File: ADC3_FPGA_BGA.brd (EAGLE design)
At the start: 40 x 40 mm, 80 parts, among them CON1 MEZZANINE_2X30, CON2 MEZZANINE_2X30, CON3 USB-SC, IC1 3.3V, IC2 MPM3804, IC3 1.0V, IC4 LFD2NX-40, IC5 EEPROM, IC6 93LC56, IC7 FT2232H, IC8 HyperRAM, J1 CLK, X1 25MHz, X2 12MHz

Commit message: Artix-7 途中
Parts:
- removed X2: 12MHz, my_rcl:KC3225
- added C36, C37, C38: 1u, my_rcl:1005
- added C39, C41, C42, C43, C47, C48, C49, C51: 0.1u, my_rcl:1608
- added C40, C46: 10u, my_rcl:1608
- added C44, C45: 22p, my_rcl:1608
- added C50: 10u, my_rcl:2012
- added D6: PWR, my_rcl:D1608
- added FB8: DRAM, my_rcl:1608-J
- added IC9: HyperRAM, my_ic:TFBGA24
- added J2: BANK35, my_rcl:2012-3-J
- added R20: 1k, my_rcl:1608
- added TP1: TMS, my_connector:TESTPAD
- added TP2: TDI, my_connector:TESTPAD
- added TP3: TCK, my_connector:TESTPAD
- added TP4: TDO, my_connector:TESTPAD
- added TP5: GND, my_connector:TESTPAD
- C10, C11, C13, C34: value 10u -> 1u; device my_rcl:2012 -> my_rcl:1005
- C12, C14, C15: value 0.1u -> 1u
- C16, C17, C18: value 0.1u -> 10u; device my_rcl:1005 -> my_rcl:1608
- C19, C4: value 0.1u -> 10u
- C2, C24: device my_rcl:1608 -> my_rcl:2012
- C20, C21, C23: value 0.1u -> 10u; device my_rcl:1005 -> my_rcl:2012
- C22, C25: value 0.1u -> 10u; device my_rcl:1608 -> my_rcl:2012
- C26, C27, C31, C32, C33, C35: value 0.1u -> 1u; device my_rcl:1608 -> my_rcl:1005
- C28, C29: value 22p -> 1u; device my_rcl:1608 -> my_rcl:1005
- C30, C9: value 10u -> 1u; device my_rcl:1608 -> my_rcl:1005
- C5: value 10u -> 0.1u
- C7, C8: device my_rcl:1608 -> my_rcl:1005
- D5: value PWR -> LED2
- FB3, IC3: value 1.0V -> 2.5V
- FB5: value FT -> 1.0V
- FB7: value DRAM -> FT
- IC1: value 3.3V -> ARTIX7-FTG256; device my_ic:SOT23-5 -> my_ic:FTG256
- IC2: value MPM3804 -> 3.3V; device my_ic:QFN-10 -> my_ic:SOT23-5
- IC4: value LFD2NX-40 -> MPM3804; device my_ic:CABGA192 -> my_ic:QFN-10
- IC5: value EEPROM -> MPM3804; device my_ic:SOP8 -> my_ic:QFN-10
- IC6: value 93LC56 -> EEPROM; device my_ic:SOT23-6 -> my_ic:SOIC-SOIJ-8
- IC7: value FT2232H -> 93LC56; device my_ic:VQFN56 -> my_ic:SOT23-6
- IC8: value HyperRAM -> FT2232H-2; device my_ic:TFBGA24 -> my_ic:QFN56-HT
- J1: value CLK -> BANK34; device my_rcl:1608-J -> my_rcl:2012-3-J
- R12, R3: value 10k -> 1k
- R13: value 1k -> 12.1k
- R14: value 12.1k -> 1k
- R4: value 10k -> 1.5k
- X1: value 25MHz -> 12MHz
- moved FB7 51.0 mm to (4.00, -22.2), flipped to the bottom, turned to 90 degrees
- moved IC8 40.3 mm to (1.50, -15.0)
- moved R7 40.3 mm to (13.5, -9.75), turned to 0 degrees
- moved C16 37.7 mm to (-7.00, -24.0), turned to 180 degrees
- moved C18 37.0 mm to (-13.0, -19.5), flipped to the top, turned to 0 degrees
- moved C9 36.1 mm to (1.00, 3.50), flipped to the bottom, turned to 0 degrees
- moved C35 34.8 mm to (7.00, 0.00)
- moved C2 32.6 mm to (-3.00, -21.5), turned to 90 degrees
- moved FB1 31.6 mm to (-2.50, -22.5), flipped to the top, turned to 270 degrees
- moved X1 31.5 mm to (9.25, -20.5), flipped to the top, turned to 0 degrees
- moved C10 31.2 mm to (1.00, 5.50), flipped to the bottom, turned to 0 degrees
- moved IC4 31.0 mm to (-13.5, -22.5), turned to 90 degrees
- moved C13 30.8 mm to (0.00, 0.50), flipped to the bottom, turned to 0 degrees
- moved C31 30.5 mm to (7.00, 7.50), turned to 0 degrees
- moved C8 30.4 mm to (3.00, -0.50), turned to 0 degrees
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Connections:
- removed net +1V0_LDO: C8.1, FB3.1, IC3.5
- removed net +3.3V_LDO: C7.1, FB2.1, IC1.5
- removed net ADC_DN1: CON1.30, IC4.H14
- removed net ADC_DP1: CON1.28, IC4.H13
- removed net INITN: IC4.B2, R8.1
- removed net JTAG_EN: IC4.A13, R7.1
- removed net N$6: J1.1, X1.3
- removed net N$7: IC2.9, R1.1, R2.2
- removed net PB10A: CON2.7, IC4.L2
- removed net PB10B: CON2.3, IC4.M2
- removed net PB12A: CON2.6, IC4.P2
- removed net PB12B: CON2.4, IC4.P3
- removed net PB4A: CON2.13, IC4.K1
- removed net PB4B: CON2.9, IC4.L1
- removed net PB58A: CON1.3, IC4.P9
- removed net PB58B: CON1.5, IC4.N9
- removed net PB60A: CON1.7, IC4.P10
- removed net PB60B: CON1.9, IC4.N10
- removed net PB64A: CON1.17, IC4.M9
- removed net PB64B: CON1.21, IC4.L9
- removed net PB66A: CON1.29, IC4.K9
- removed net PB66B: CON1.27, IC4.K10
- removed net PB68A: CON1.15, IC4.M11
- removed net PB68B: CON1.19, IC4.L12
- removed net PB6A: CON2.12, IC4.K3
- removed net PB6B: CON2.10, IC4.L3
- removed net PB70A: CON1.25, IC4.K11
- removed net PB70B: CON1.23, IC4.K12
- removed net PB72A: CON1.11, IC4.P11
- removed net PB72B: CON1.13, IC4.N11
- removed net PB74A: CON1.4, IC4.P12
- removed net PB74B: CON1.6, IC4.P13
- removed net PB76A: CON1.8, IC4.N13
- removed net PB76B: CON1.10, IC4.N14
- removed net PB78A: CON1.14, IC4.M14
- removed net PB78B: CON1.12, IC4.M13
- removed net PB80A: CON1.16, IC4.L13
- removed net PB80B: CON1.18, IC4.L14
- removed net PB82A: CON1.20, IC4.K13
- removed net PB82B: CON1.22, IC4.K14
- removed net PB84A: CON1.26, IC4.J14
- removed net PB84B: CON1.24, IC4.J13
- removed net PB8A: CON2.5, IC4.M1
- removed net PB8B: CON2.8, IC4.N1
- removed net PL24A: CON2.30, IC4.E2
- removed net PL24B: CON2.32, IC4.E1
- removed net PL26A: CON2.28, IC4.F3
- removed net PL26B: CON2.26, IC4.F4
- removed net PL30A: CON2.29, IC4.F2, J1.2
- removed net PL30B: CON2.31, IC4.F1
- removed net PL32A: CON2.27, IC4.G1
- removed net PL32B: CON2.25, IC4.G2
- removed net PL36A: CON2.23, IC4.H1
- removed net PL36B: CON2.21, IC4.H2
- removed net PL38A: CON2.24, IC4.H3
- removed net PL38B: CON2.22, IC4.H4
- removed net PL42A: CON2.19, IC4.J1
- removed net PL42B: CON2.17, IC4.J2
- removed net PL44A: CON2.20, IC4.J3
- removed net PL44B: CON2.18, IC4.J4
- removed net PL47A: CON2.11, IC4.K2
- removed net PR13B: CON1.51, IC4.A12
- removed net PR17A: CON1.49, IC4.A10
- removed net PR24A: CON1.46, IC4.D14
- removed net PR24B: CON1.50, IC4.C14
- removed net PR26A: CON1.47, IC4.C11
- removed net PR27A: CON1.48, IC4.D12
- removed net PR27B: CON1.39, IC4.E12
- removed net PR30A: CON1.45, IC4.E9
- removed net PR30B: CON1.41, IC4.E10
- removed net PR32A: CON1.43, IC4.D11
- removed net PR32B: CON1.37, IC4.E11
- removed net PR34A: CON1.40, IC4.F13
- removed net PR34B: CON1.38, IC4.F14
- removed net PR36A: CON1.44, IC4.E13
- removed net PR36B: CON1.42, IC4.E14
- removed net PR38A: CON1.34, IC4.G14
- removed net PR38B: CON1.36, IC4.G13
- removed net PR42A: CON1.35, IC4.F11
- removed net PR42B: CON1.33, IC4.G12
- removed net PROGRAMN: IC4.A2, R9.1
- new net +1V0_DCDC: C19.1, FB5.1, IC5.6, IC5.7, IC5.8, R3.2
- new net +1V0_DCDC_FB: IC5.9, R3.1, R4.2
- new net +1V8_DCDC_FB: IC4.9, R1.1, R2.2
- new net +2V5: C21.1, CON2.49, CON2.50, FB3.2, J1.3, J2.3
- new net +2V5_LDO: C17.1, FB3.1, IC3.5
- new net +3V3_LDO: C16.1, FB2.1, IC2.5
- new net 1.0V_DCDC_SW: IC5.2, IC5.3, IC5.4
- new net INIT_B: IC1.K10, R7.1
- new net IO0_14: CON2.26, IC1.K12
- new net IO10N_15: CON2.7, IC1.B16
- new net IO10N_35: CON1.16, IC1.D1
- new net IO10P_15: CON2.9, IC1.C16
- new net IO10P_35: CON1.18, IC1.E2
- new net IO11N_14: CON2.40, IC1.P13
- new net IO11P_14: CON2.38, IC1.N13
- new net IO12N_14: CON2.32, IC1.P14
- new net IO12N_35: CON1.19, IC1.C4
- new net IO12P_14: CON2.30, IC1.N14
- new net IO12P_35: CON1.21, IC1.D4
- new net IO13N_15: CON2.12, IC1.E13
- new net IO13P_15: CON2.14, IC1.E12
- new net IO14N_35: CON1.23, IC1.F3
- new net IO14P_35: CON1.25, IC1.F4
- new net IO15N_15: CON2.10, IC1.D15
- new net IO15N_35: CON1.20, IC1.E1
- new net IO15P_15: CON2.8, IC1.D14
- new net IO15P_35: CON1.22, IC1.F2
- new net IO17N_15: CON2.11, IC1.D16
- new net IO17N_35: CON1.24, IC1.G1
- new net IO17P_15: CON2.13, IC1.E16
- new net IO17P_35: CON1.26, IC1.G2
- new net IO19N_35: CON1.35, IC1.J4
- new net IO19P_35: CON1.37, IC1.J5
- new net IO20N_35: CON1.28, IC1.H1
- new net IO20P_35: CON1.30, IC1.H2
- new net IO21N_15: CON2.16, IC1.F14
- new net IO21N_35: CON1.27, IC1.H3
- new net IO21P_15: CON2.18, IC1.G14
- new net IO21P_35: CON1.29, IC1.J3
- new net IO22N_15: CON2.15, IC1.G16
- new net IO22N_35: CON1.32, IC1.J1
- new net IO22P_15: CON2.17, IC1.H16
- new net IO22P_35: CON1.34, IC1.K1
- new net IO23N_15: CON2.21, IC1.J16
- new net IO23N_35: CON1.38, IC1.L2
- new net IO23P_15: CON2.19, IC1.J15
- new net IO23P_35: CON1.36, IC1.L3
- new net IO24N_15: CON2.20, IC1.G15
- new net IO24N_35: CON1.31, IC1.K2
- new net IO24P_15: CON2.22, IC1.H14
- new net IO24P_35: CON1.33, IC1.K3
- new net IO2N_14: CON2.27, IC1.K16
- new net IO2N_34: CON1.42, IC1.M1
- new net IO2N_35: CON1.9, IC1.B5
- new net IO2P_14: CON2.25, IC1.K15
- new net IO2P_34: CON1.44, IC1.M2
- new net IO2P_35: CON1.7, IC1.B6
- new net IO3N_35: CON1.6, IC1.A4
- new net IO3P_35: CON1.4, IC1.A5
- new net IO4N_14: CON2.31, IC1.M14
- new net IO4N_34: CON1.48, IC1.P1
- new net IO4N_35: CON1.11, IC1.A3
- new net IO4P_14: CON2.29, IC1.L14
- new net IO4P_34: CON1.46, IC1.N1
- new net IO4P_35: CON1.13, IC1.B4
- new net IO5N_34: CON1.43, IC1.P3
- new net IO5N_35: CON1.5, IC1.C6
- new net IO5P_14: CON2.28, IC1.K13
- new net IO5P_34: CON1.41, IC1.P4
- new net IO5P_35: CON1.3, IC1.C7
- new net IO7N_14: CON2.35, IC1.N16
- new net IO7N_34: CON1.50, IC1.R1
- new net IO7N_35: CON1.15, IC1.C2
- new net IO7P_14: CON2.33, IC1.M16
- new net IO7P_34: CON1.52, IC1.R2
- new net IO7P_35: CON1.17, IC1.C3
- new net IO8N_14: CON2.39, IC1.P16
- new net IO8N_15: CON2.4, IC1.B14
- new net IO8N_34: CON1.47, IC1.T2
- new net IO8N_35: CON1.8, IC1.A2
- new net IO8P_14: CON2.37, IC1.P15
- new net IO8P_15: CON2.6, IC1.C14
- new net IO8P_34: CON1.45, IC1.R3
- new net IO8P_35: CON1.10, IC1.B2
- new net IO9N_14: CON2.36, IC1.R16
- new net IO9N_15: CON2.3, IC1.A15
- new net IO9N_34: CON1.49, IC1.T3
- new net IO9N_35: CON1.12, IC1.B1
- new net IO9P_14: CON2.34, IC1.R15
- new net IO9P_15: CON2.5, IC1.B15
- new net IO9P_34: CON1.51, IC1.T4
- new net IO9P_35: CON1.14, IC1.C1
- new net LED3: D5.A, IC1.R5
- new net N$5: D5.K, R18.2
- new net PROGRAM_B: IC1.L9, R8.1
- new net VCCO34: C24.1, C26.1, C28.1, IC1.M3, IC1.R4, IC1.T1, J1.2
- new net VCCO35: C25.1, C27.1, C29.1, C30.1, IC1.A6, IC1.B3, IC1.D7, IC1.E4, IC1.F1, IC1.J2, J2.2
- net +1V0: now also C13.1, C23.1, C7.1, C9.1, FB5.2, IC1.E10, IC1.F11, IC1.F7, IC1.F9, IC1.G6, IC1.H9, IC1.J6, IC1.K9, IC1.L8; no longer C12.1, C17.1, FB3.2, IC4.F9, IC4.G7, IC4.H9, IC4.J7, IC4.J9
- net +1V8: now also C10.1, C12.1, C22.1, C31.1, C33.1, C35.1, C8.1, FB7.1, FB8.2, IC1.A16, IC1.B13, IC1.C10, IC1.E14, IC1.G10, IC1.G8, IC1.H15, IC1.J10, IC1.J12, IC1.K11, IC1.L10; no longer C13.1, C16.1, C18.1, C23.1, C6.1, FB6.1, FB7.2, IC3.1, IC3.3, IC4.F7, IC4.G9, IC4.H10, IC4.H7, IC4.J10, IC4.J12, IC4.L11, IC4.L5, IC4.M10, IC4.M3, IC4.M6, IC4.N12, IC4.N3
- net +1V8_DCDC: now also C18.1, IC4.6, IC4.7, IC4.8; no longer C9.1, IC2.6, IC2.7, IC2.8
- net +3V3: now also C32.1, C34.1, C36.1, C37.1, C38.1, C39.1, D6.A, FB6.1, IC1.E7, IC1.L15, IC1.L16, IC1.L6, IC1.M13, IC1.M9, IC1.N10, IC1.P7, IC1.R14, IC1.T11, IC6.3, IC6.7, IC6.8, J1.1, J2.1, R5.2; no longer C10.1, C19.1, C21.1, C22.1, CON2.49, CON2.50, D5.A, FB5.1, IC4.C12, IC4.C7, IC4.E4, IC4.G11, IC4.G4, IC5.3, IC5.7, IC5.8, R11.2, R3.2, R4.2, X1.1, X1.4
- net 1.8V_DCDC_SW: now also IC4.2, IC4.3, IC4.4; no longer IC2.2, IC2.3, IC2.4
- net DONE: now also IC1.H10, R9.1; no longer IC4.A3, R10.1
- net DRAM_+1V8: now also C49.1, C50.1, C51.1, FB8.1, IC9.B4, IC9.D1, IC9.E4, R20.2; no longer C33.1, C34.1, C35.1, FB7.1, IC8.B4, IC8.D1, IC8.E4
- net DRAM_CKN: now also IC1.A9, IC9.B1; no longer IC4.L7, IC8.B1
- net DRAM_CKP: now also IC1.A8, IC9.B2; no longer IC4.M7, IC8.B2
- net DRAM_CS: now also IC1.C8, IC9.A3; no longer IC4.K6, IC8.A3
- net DRAM_DQ0: now also IC1.A10, IC9.D3; no longer IC4.N5, IC8.D3
- net DRAM_DQ1: now also IC1.B11, IC9.D2; no longer IC4.P7, IC8.D2
- net DRAM_DQ2: now also IC1.A13, IC9.C4; no longer IC4.P4, IC8.C4
- net DRAM_DQ3: now also IC1.C13, IC9.D4; no longer IC4.N4, IC8.D4
- net DRAM_DQ4: now also IC1.A14, IC9.D5; no longer IC4.M4, IC8.D5
- net DRAM_DQ5: now also IC1.C12, IC9.E3; no longer IC4.P5, IC8.E3
- net DRAM_DQ6: now also IC1.A12, IC9.E2; no longer IC4.P6, IC8.E2
- net DRAM_DQ7: now also IC1.B12, IC9.E1; no longer IC4.N6, IC8.E1
- net DRAM_NRST: now also IC9.A4, R20.1; no longer IC4.K5, IC8.A4
- net DRAM_RWDS: now also IC1.B10, IC9.C3; no longer IC4.N7, IC8.C3
- net FLASH_CS: now also IC1.L12, IC6.1, R10.1; no longer IC4.B4, IC5.1, R11.1
- net FLASH_MISO: now also IC1.J14, IC6.2; no longer IC4.A5, IC5.2
- net FLASH_MOSI: now also IC1.J13, IC6.5; no longer IC4.A4, IC5.5
- net FLASH_SCK: now also IC1.E8, IC6.6; no longer IC4.B3, IC5.6
- net FT_+1V8: now also C46.1, C47.1, C48.1, FB7.2, IC8.2, IC8.31; no longer C30.1, C31.1, C32.1, FB6.2, IC7.2, IC7.31
- net FT_+3V3: now also C40.1, C41.1, C42.1, C43.1, FB6.2, IC7.6, IC8.16, IC8.36, IC8.5, IC8.50, IC8.9, R11.1, R14.1; no longer C24.1, C25.1, C26.1, C27.1, FB5.2, IC6.6, IC7.16, IC7.36, IC7.5, IC7.50, IC7.9, R12.1, R15.1
- net FT_CLK: now also IC1.N11, IC8.27; no longer IC4.D7, IC7.27
- net FT_D0: now also IC1.T15, IC8.12; no longer IC4.E3, IC7.12
- net FT_D1: now also IC1.T14, IC8.13; no longer IC4.D2, IC7.13
- net FT_D2: now also IC1.R13, IC8.14; no longer IC4.D1, IC7.14
- net FT_D3: now also IC1.T13, IC8.15; no longer IC4.D3, IC7.15
- net FT_D4: now also IC1.R12, IC8.17; no longer IC4.C1, IC7.17
- net FT_D5: now also IC1.T12, IC8.18; no longer IC4.C2, IC7.18
- net FT_D6: now also IC1.R11, IC8.19; no longer IC4.B1, IC7.19
- net FT_D7: now also IC1.R10, IC8.20; no longer IC4.C3, IC7.20
- net FT_NOE: now also IC1.T7, IC8.28; no longer IC4.D6, IC7.28
- net FT_NRD: now also IC1.P8, IC8.24; no longer IC4.C5, IC7.24
- net FT_NWR: now also IC1.T8, IC8.25; no longer IC4.C6, IC7.25
- net FT_RXNF: now also IC1.T10, IC8.22; no longer IC4.C4, IC7.22
- net FT_SIWU: now also IC1.R8, IC8.26; no longer IC4.D5, IC7.26
- net FT_TXNE: now also IC1.T9, IC8.23; no longer IC4.B5, IC7.23
- net GND: now also C36.2, C37.2, C38.2, C39.2, C40.2, C41.2, C42.2, C43.2, C44.2, C45.2, C46.2, C47.2, C48.2, C49.2, C50.2, C51.2, CON1.39, CON1.40, CON2.23, CON2.24, IC1.A1, IC1.A11, IC1.B8, IC1.C15, IC1.C5, IC1.D12, IC1.D2, IC1.E9, IC1.F10, IC1.F16, IC1.F6, IC1.F8, IC1.G13, IC1.G3, IC1.G7, IC1.G9, IC1.H6, IC1.H7, IC1.H8, IC1.J11, IC1.J7, IC1.J8, IC1.J9, IC1.K14, IC1.K4, IC1.K6, IC1.K7, IC1.K8, IC1.L1, IC1.L11, IC1.M10, IC1.M11, IC1.M8, IC1.N15, IC1.N5, IC1.P12, IC1.P2, IC1.R9, IC1.T16, IC1.T6, IC2.2, IC4.10, IC5.10, IC6.4, IC7.2, IC8.10, IC8.21, IC8.41, IC8.45, IC8.HT, IC9.B3, IC9.C1, IC9.E5, R13.2, R15.1, R4.1, TP5.1, X1.4; no longer CON1.31, CON1.32, CON1.52, CON2.14, CON2.15, CON2.16, CON2.33, CON2.34, CON2.35, CON2.36, CON2.37, CON2.38, CON2.39, CON2.40, IC1.2, IC2.10, IC4.A1, IC4.A14, IC4.B11, IC4.B6, IC4.D4, IC4.F12, IC4.F8, IC4.G3, IC4.G8, IC4.H8, IC4.J11, IC4.J8, IC4.L10, IC4.M12, IC4.M5, IC4.N2, IC4.P1, IC4.P14, IC5.4, IC6.2, IC7.10, IC7.21, IC7.41, IC7.45, IC7.HT, IC8.B3, IC8.C1, IC8.E5, R14.2, R5.1, X2.2, X2.4
- net JTAG_TCK: now also IC1.L7, IC8.32, TP3.1; no longer IC4.A11, IC7.32, R5.2
- net JTAG_TDI: now also IC1.N7, IC8.33, R5.1, TP2.1; no longer IC4.D9, IC7.33, R4.1
- net JTAG_TDO: now also IC1.N8, IC8.34, TP4.1; no longer IC4.D10, IC7.34, R3.1
- net JTAG_TMS: now also IC1.M7, IC8.35, TP1.1; no longer IC4.E8, IC7.35
- net LED0: now also IC1.R7; no longer IC4.B13
- net LED1: now also IC1.R6; no longer IC4.B14
- net LED2: now also IC1.T5; no longer IC4.B12
- net N$1: now also D6.K; no longer D5.K
- net N$10: now also IC7.3, IC8.55, R12.2; no longer IC6.3, IC7.55, R13.2
- net N$11: now also IC7.5, IC8.1; no longer IC6.5, IC7.1
- net N$12: now also IC7.1, R11.2, R12.1; no longer IC6.1, R12.2, R13.1
- net N$13: now also C45.1, IC8.4, X1.3; no longer C29.1, IC7.4, X2.3
- net N$14: now also C44.1, IC8.3, X1.1; no longer C28.1, IC7.3, X2.1
- net N$15: now also IC8.6, R13.1; no longer IC7.6, R14.1
- net N$16: now also IC8.11, R14.2; no longer IC7.11, R15.2
- net N$2: now also R15.2; no longer R16.2
- net N$3: now also R16.2; no longer R17.2
- net N$4: now also R17.2; no longer R18.2
- net N$9: now also IC7.4, IC8.56; no longer IC6.4, IC7.56
- net USB_DM: now also IC8.7; no longer IC7.7
- net USB_DP: now also IC8.8; no longer IC7.8
- net VIN_DCDC: now also C6.1, IC2.3, IC3.1, IC3.3, IC4.1, IC4.5, IC5.1, IC5.5; no longer IC1.1, IC1.3, IC2.5
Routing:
- net +1V8: track 242.0 -> 69.9 mm, vias 24 -> 13
- net +3V3: track 223.2 -> 95.1 mm, vias 11 -> 14
- net VIN: track 96.2 -> 0.00 mm, vias 4 -> 0
- net VCCO35: track 0.00 -> 32.1 mm, vias 0 -> 7
- net FT_+3V3: track 73.1 -> 44.5 mm, vias 8 -> 6
- net FLASH_SCK: track 11.7 -> 37.4 mm
- net +2V5: track 0.00 -> 25.2 mm, vias 0 -> 2
- net VCCO34: track 0.00 -> 23.7 mm, vias 0 -> 4
- net VIN_DCDC: track 24.9 -> 47.1 mm, vias 3 -> 4
- net INIT_B: track 0.00 -> 20.4 mm, vias 0 -> 2
- net PROGRAMN: track 19.9 -> 0.00 mm, vias 2 -> 0
- net PROGRAM_B: track 0.00 -> 17.8 mm, vias 0 -> 2
- net INITN: track 17.8 -> 0.00 mm, vias 2 -> 0
- net FLASH_MISO: track 13.3 -> 31.0 mm
- net FT_+1V8: track 45.7 -> 28.3 mm, vias 3 -> 2
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- removed copper zone on layer 2, net GND
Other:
- board size 40 x 40 mm -> 40.2 x 45 mm

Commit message: via打てば終わり
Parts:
- D2: value LED0 -> 0
- D3: value LED1 -> 1
- D4: value LED2 -> 2
- D5: value LED2 -> 3
- D6: value PWR -> P
- IC8: value FT2232H-2 -> FT2232H
- moved FB7 14.0 mm to (-5.50, -12.0), turned to 180 degrees
- moved C1 4.75 mm to (17.0, -22.8)
- moved D1 3.26 mm to (13.0, -22.8), turned to 180 degrees
- moved FB3 2.70 mm to (-17.8, -21.5)
- moved FB6 1.41 mm to (0.75, -21.2), turned to 180 degrees
- moved C28 1.25 mm to (-5.00, -3.75)
- moved C50 0.75 mm to (8.25, 13.5)
- moved FB1 0.50 mm to (-3.00, -22.5), turned to 90 degrees
- moved C5 0.25 mm to (-7.00, -18.0)
- moved C6 0.25 mm to (-13.0, -18.0)
- moved FB2 0.25 mm to (-9.75, -22.8)
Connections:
- net +1V8: no longer CON1.55, CON1.56
- net +2V5: now also CON1.55, CON1.56; no longer CON2.49, CON2.50
- net +3V3: now also CON2.49, CON2.50
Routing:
- net VIN: track 0.00 -> 45.5 mm, vias 0 -> 1
- net +1V8: track 69.9 -> 31.3 mm, vias 13 -> 17
- net +1V0: track 36.4 -> 4.79 mm, vias 10 -> 11
- net +3V3: track 95.1 -> 64.5 mm, vias 14 -> 22
- net VCCO35: track 32.1 -> 6.66 mm
- net VCCO34: track 23.7 -> 5.06 mm
- net USB_+5V: track 0.00 -> 5.43 mm, vias 0 -> 2
- net +2V5_LDO: track 3.42 -> 6.30 mm
- net +2V5: track 25.2 -> 22.7 mm, vias 2 -> 3
- net FLASH_CS: track 31.8 -> 33.9 mm
- net IO8P_14: track 13.5 -> 14.9 mm
- net IO8N_14: track 12.2 -> 13.6 mm
- net IO4P_14: track 14.6 -> 16.0 mm
- net IO4N_14: track 14.7 -> 16.1 mm
- added copper zone on layer 3, net +1V0
- added copper zone on layer 14, net +1V8
- added copper zone on layer 3, net +2V5
- added copper zone on layer 14, net +3V3
- added copper zone on layer 2, net GND
- added copper zone on layer 3, net VCCO34
- added copper zone on layer 3, net VCCO35
- removed copper zone on layer 14, net GND
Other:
- board size 40.2 x 45 mm -> 40.4 x 44.4 mm
- board text added: "FPGA Core Board ver2"
- board text removed: "FPGA Core Board ver1"

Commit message: 発注
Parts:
- added C52, C53, C54: 10u, my_rcl:2012
- C11, C12: value 1u -> 0.1u; device my_rcl:1005 -> my_rcl:1608
- C16, C4: value 10u -> 1u; device my_rcl:1608 -> my_rcl:1005
- C20: device my_rcl:2012 -> my_rcl:1608
- C26: value 1u -> 10u; device my_rcl:1005 -> my_rcl:2012
- C39, C5: value 0.1u -> 1u; device my_rcl:1608 -> my_rcl:1005
- C40: value 10u -> 0.1u
- C41, C47, C6: value 0.1u -> 10u
- C44: value 22p -> 0.1u
- C46: value 10u -> 22p
- C50: value 10u -> 0.1u; device my_rcl:2012 -> my_rcl:1608
- R11: value 10k -> 1k
- R13: value 12.1k -> 10k
- R17: value 1k -> 12.1k
- moved C49 31.5 mm to (4.50, -18.0), turned to 0 degrees
- moved C16 27.2 mm to (-1.00, 2.50)
- moved C12 25.2 mm to (-13.0, -18.0), turned to 0 degrees
- moved R18 24.3 mm to (9.00, -13.0), turned to 180 degrees
- moved C4 23.6 mm to (-2.50, -1.00), flipped to the bottom, turned to 270 degrees
- moved R14 22.6 mm to (-13.5, -15.0), turned to 90 degrees
- moved R17 22.5 mm to (9.00, -16.2), turned to 0 degrees
- moved C39 21.7 mm to (1.50, -4.25), turned to 90 degrees
- moved C5 20.2 mm to (3.00, -0.50)
- moved C11 19.9 mm to (-7.00, -18.0)
- moved C25 18.7 mm to (-13.0, -17.8)
- moved C23 17.4 mm to (-17.2, -4.50)
- moved C32 15.5 mm to (7.00, 7.50), turned to 0 degrees
- moved R12 15.1 mm to (-11.8, -15.0), turned to 90 degrees
- moved R16 15.1 mm to (1.50, -22.2), turned to 270 degrees
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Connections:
- net +1V0: now also C16.1, C26.1, C4.1, C53.1; no longer C11.1, C23.1
- net +1V0_DCDC: now also C20.1; no longer C19.1
- net +1V8: now also C25.1, C32.1, C34.1, C36.1, C5.1, C54.1; no longer C12.1, C22.1, C31.1, C33.1, C35.1
- net +1V8_DCDC: now also C19.1; no longer C18.1
- net +2V5: now also C22.1; no longer C21.1
- net +2V5_LDO: now also C18.1; no longer C17.1
- net +3V3: now also C21.1, C33.1, C35.1, C40.1; no longer C20.1, C32.1, C34.1, C36.1
- net +3V3_LDO: now also C17.1; no longer C16.1
- net DRAM_+1V8: now also C52.1; no longer C49.1
- net FT_+1V8: now also C49.1; no longer C46.1
- net FT_+3V3: now also C44.1, R13.1, R18.1; no longer C40.1, R11.1, R14.1
- net GND: now also C52.2, C53.2, C54.2, R11.1, R12.1, R14.1, R17.2; no longer R13.2, R16.1, R17.1, R18.1
- net N$10: now also R16.2; no longer R12.2
- net N$12: now also R13.2, R16.1; no longer R11.2, R12.1
- net N$13: now also C46.1; no longer C45.1
- net N$14: now also C45.1; no longer C44.1
- net N$15: now also R17.1; no longer R13.1
- net N$16: now also R18.2; no longer R14.2
- net N$2: now also R11.2; no longer R15.2
- net N$3: now also R12.2; no longer R16.2
- net N$4: now also R14.2; no longer R17.2
- net N$5: now also R15.2; no longer R18.2
- net VCCO34: now also C23.1, C27.1, C29.1; no longer C24.1, C26.1, C28.1
- net VCCO35: now also C24.1, C28.1, C31.1; no longer C25.1, C27.1, C29.1
- net VIN_DCDC: now also C11.1, C12.1; no longer C4.1, C5.1
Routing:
- net +1V8: track 31.3 -> 34.1 mm
- net +1V0: track 4.79 -> 7.57 mm

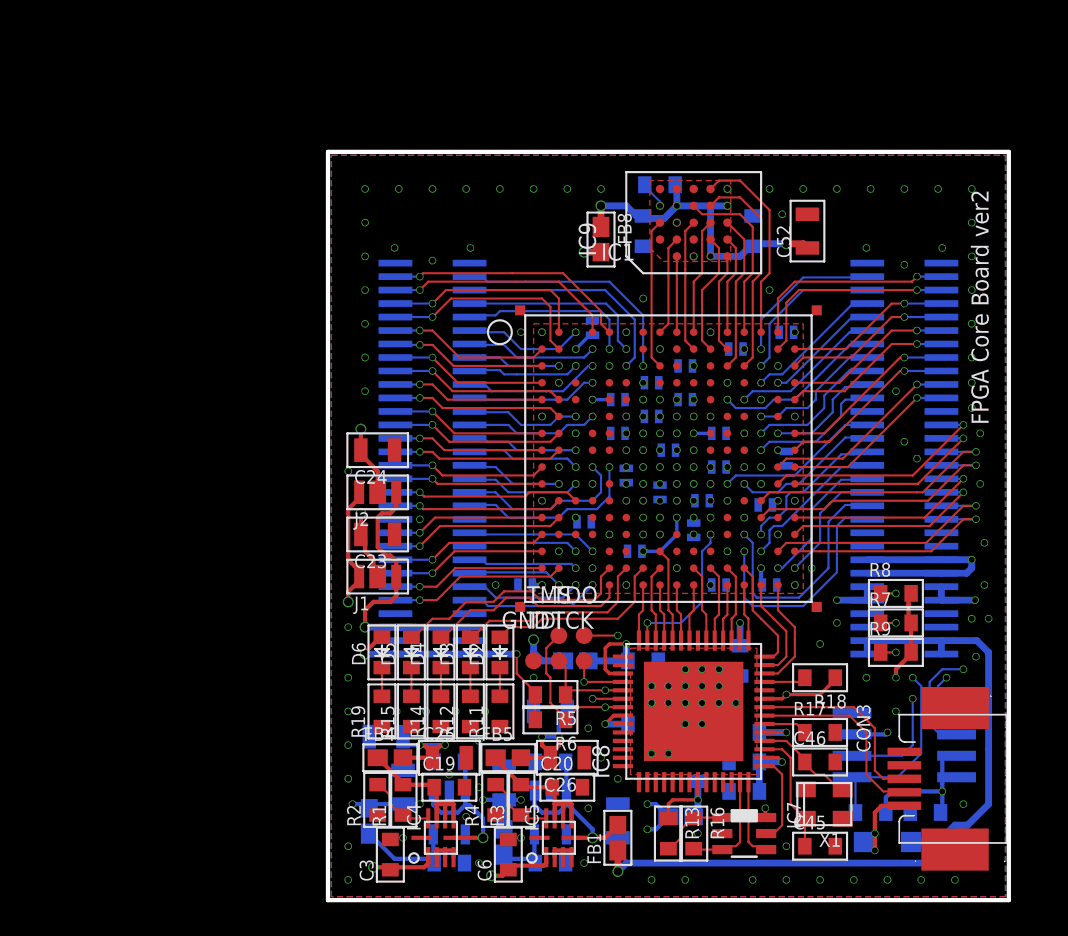
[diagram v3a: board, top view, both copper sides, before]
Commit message: OSCを追加して再発注
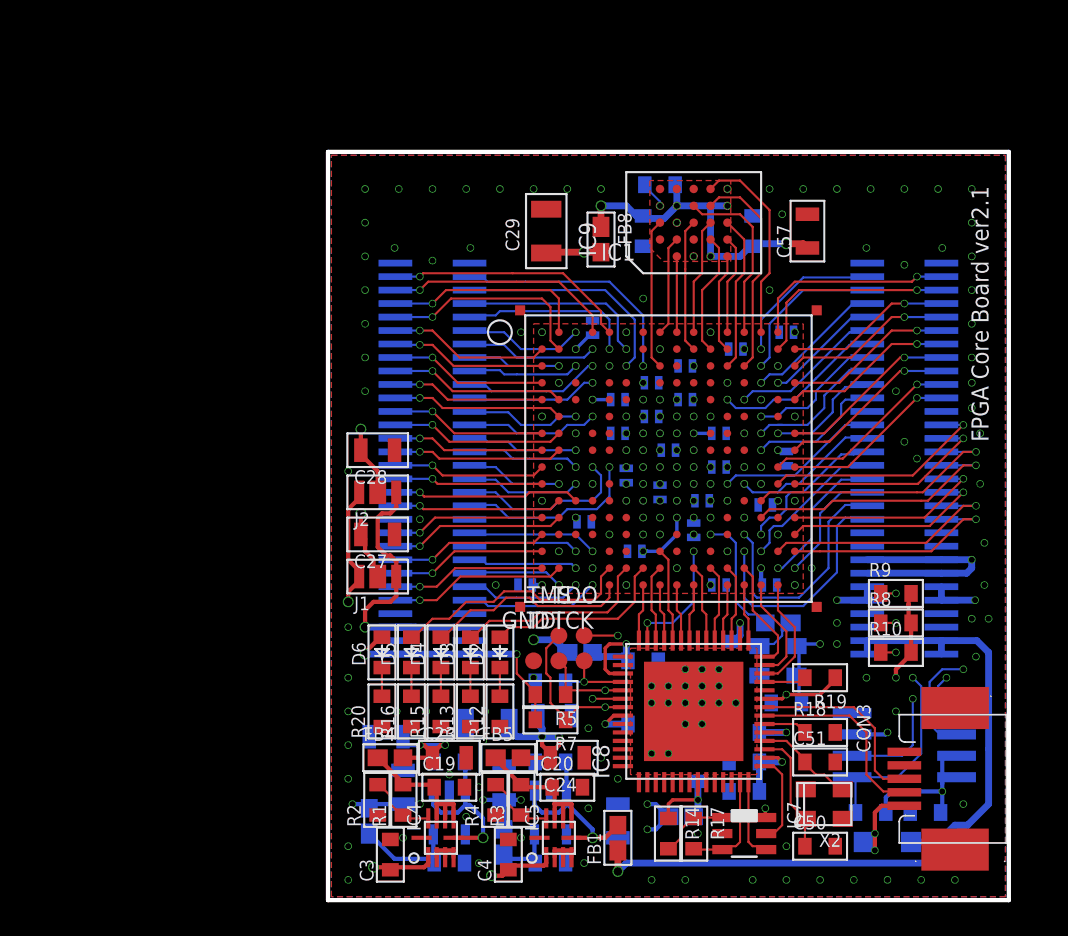
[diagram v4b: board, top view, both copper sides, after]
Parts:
- added C55, C56: 0.1u, my_rcl:1608
- added C57: 10u, my_rcl:2012
- added J3: 25M, my_rcl:1608-J
- added R21: 1k, my_rcl:1608
- added X2: 12MHz, my_rcl:KC3225
- C10, C9: value 1u -> 0.1u; device my_rcl:1005 -> my_rcl:1608
- C11, C12, C40, C42, C43: value 0.1u -> 1u; device my_rcl:1608 -> my_rcl:1005
- C27, C28: value 1u -> 10u; device my_rcl:1005 -> my_rcl:2012
- C29, C30: value 1u -> 10u; device my_rcl:1005 -> my_rcl:3216
- C4: value 1u -> 10u; device my_rcl:1005 -> my_rcl:1608
- C41, C6: value 10u -> 1u; device my_rcl:1608 -> my_rcl:1005
- C45: value 22p -> 0.1u
- C46: value 22p -> 10u
- C47: value 10u -> 0.1u
- C50, C51: value 0.1u -> 22p
- C52: device my_rcl:2012 -> my_rcl:1608
- C53, C54: value 10u -> 0.1u; device my_rcl:2012 -> my_rcl:1608
- R11, R14: value 1k -> 10k
- R13: value 10k -> 1k
- R17: value 12.1k -> 1k
- R18: value 1k -> 12.1k
- X1: value 12MHz -> 25MHz
- moved C50 36.7 mm to (9.00, -23.0), flipped to the top, turned to 0 degrees
- moved R20 35.3 mm to (-17.0, -15.0), flipped to the top, turned to 90 degrees
- moved C52 33.5 mm to (4.50, -19.8), flipped to the bottom, turned to 0 degrees
- moved C51 33.2 mm to (9.00, -18.0), flipped to the top, turned to 0 degrees
- moved C6 26.2 mm to (3.00, -0.50), flipped to the bottom, turned to 0 degrees
- moved R19 26.1 mm to (9.00, -13.0), turned to 180 degrees
- moved C10 25.2 mm to (-13.0, -18.0), turned to 0 degrees
- moved C12 25.2 mm to (3.00, 1.50), turned to 180 degrees
- moved C4 23.6 mm to (-9.50, -23.5), flipped to the top, turned to 90 degrees
- moved R11 22.8 mm to (12.0, -21.0), flipped to the bottom, turned to 180 degrees
- moved C40 22.6 mm to (7.00, 0.00), turned to 270 degrees
- moved C30 22.5 mm to (-10.8, -15.8), turned to 0 degrees
- moved C24 21.4 mm to (-6.00, -17.8)
- moved C54 21.3 mm to (4.50, -18.0)
- moved R7 21.3 mm to (-7.00, -15.5), turned to 180 degrees
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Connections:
- new net CLK_25M: IC1.N11, J3.2
- new net N$8: J3.1, X1.3
- net +1V0: now also C11.1, C24.1, C30.1, C5.1; no longer C4.1, C53.1, C9.1
- net +1V8: now also C12.1, C23.1, C29.1, C38.1, C40.1, C6.1; no longer C10.1, C32.1, C34.1, C5.1, C54.1
- net +3V3: now also C41.1, C42.1, C43.1, C44.1, C45.1, R11.2, X1.1, X1.4; no longer C33.1, C35.1, C38.1, C40.1, R6.2
- net DONE: now also R10.1; no longer R9.1
- net DRAM_+1V8: now also C55.1, C56.1, C57.1, R21.2; no longer C50.1, C51.1, C52.1, R20.2
- net DRAM_NRST: now also R21.1; no longer R20.1
- net FLASH_CS: now also R11.1; no longer R10.1
- net FT_+1V8: now also C52.1, C53.1, C54.1; no longer C47.1, C48.1, C49.1
- net FT_+3V3: now also C46.1, C47.1, C48.1, C49.1, R14.1, R19.1; no longer C41.1, C42.1, C43.1, C44.1, R13.1, R18.1
- net FT_CLK: now also IC1.P10; no longer IC1.N11
- net GND: now also C55.2, C56.2, C57.2, R13.1, R16.1, R18.2, R20.1, R6.1, X2.2, X2.4; no longer R11.1, R14.1, R17.2, R19.1, X1.4
- net INIT_B: now also R8.1; no longer R7.1
- net JTAG_TCK: now also R6.2
- net JTAG_TMS: now also R7.1; no longer R6.1
- net N$1: now also R20.2; no longer R19.2
- net N$10: now also R17.2; no longer R16.2
- net N$12: now also R14.2, R17.1; no longer R13.2, R16.1
- net N$13: now also C51.1, X2.3; no longer C46.1, X1.3
- net N$14: now also C50.1, X2.1; no longer C45.1, X1.1
- net N$15: now also R18.1; no longer R17.1
- net N$16: now also R19.2; no longer R18.2
- net N$2: now also R12.2; no longer R11.2
- net N$3: now also R13.2; no longer R12.2
- net N$4: now also R15.2; no longer R14.2
- net N$5: now also R16.2; no longer R15.2
- net PROGRAM_B: now also R9.1; no longer R8.1
- net VCCO34: now also C31.1, C33.1; no longer C23.1, C29.1
- net VCCO35: now also C32.1, C34.1, C35.1; no longer C24.1, C30.1, C31.1
- net VIN_DCDC: now also C10.1, C4.1, C9.1; no longer C11.1, C12.1, C6.1
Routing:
- net CLK_25M: track 0.00 -> 7.47 mm, vias 0 -> 1
- net +3V3: track 64.5 -> 69.6 mm, vias 22 -> 23
- net N$8: track 0.00 -> 2.57 mm
- net +1V0: track 7.57 -> 9.65 mm
- net +1V8: track 34.1 -> 36.0 mm
- net FT_CLK: track 9.02 -> 7.32 mm
- net JTAG_TCK: track 15.7 -> 16.8 mm
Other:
- board text added: "FPGA Core Board ver2.1"
- board text removed: "FPGA Core Board ver2"

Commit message: Type-C
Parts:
- removed C30: 10u, my_rcl:3216
- added R22, R23: 5.1k, my_rcl:1608
- C1, C10, C17, C18, C19, C20, C3, C4, C44, C45, C46, C47, C48, C49, C50, C51, C52, C53, C54, C55, C56, C9: device my_rcl:1608 -> my_rcl:1608C
- CON3: value USB-SC -> USB-C; device my_connector:UX60SC-MB-5ST -> my_connector:5077CR-16-SMC2-BK-TR
- J1, J2: device my_rcl:2012-3-J -> my_rcl:1608-3-J
- TP1, TP2, TP3, TP4, TP5: device my_connector:TESTPAD -> my_connector:TESTPAD-SMALL
- moved C1 11.8 mm to (5.25, -23.0), turned to 90 degrees
- moved D1 3.13 mm to (10.2, -24.2), turned to 0 degrees
- moved CON3 3.01 mm to (13.2, -18.8), turned to 90 degrees
- moved C44 2.06 mm to (17.2, -21.5), turned to 180 degrees
- moved IC6 0.79 mm to (14.2, -17.8)
- moved C22 0.75 mm to (-15.8, -20.2)
- moved C25 0.75 mm to (-16.8, -17.2)
- moved R11 0.71 mm to (11.5, -21.5)
- moved FB3 0.25 mm to (-17.8, -21.8)
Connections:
- new net N$6: CON3.A5:CC1, R22.2
- new net N$7: CON3.B5:CC2, R23.2
- net +1V0: no longer C30.1
- net GND: now also CON3.A1,B12:GND, CON3.B1,A12:GND, CON3.SHILED1, CON3.SHILED2, CON3.SHILED3, CON3.SHILED4, CON3.SHILED5, CON3.SHILED6, CON3.SHILED7, CON3.SHILED8, R22.1, R23.1; no longer C30.2, CON3.5, CON3.M1, CON3.M2
- net USB_+5V: now also CON3.A4,B9:VBUS, CON3.B4,A9:VBUS; no longer CON3.1
- net USB_DM: now also CON3.A7:DN1, CON3.B7:DN2; no longer CON3.2
- net USB_DP: now also CON3.A6:DP1, CON3.B6:DP2; no longer CON3.3
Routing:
- net N$7: track 0.00 -> 9.98 mm, vias 0 -> 2
- net N$6: track 0.00 -> 9.88 mm, vias 0 -> 2
- net USB_+5V: track 5.91 -> 9.90 mm, vias 2 -> 4
- net +1V0: track 9.65 -> 6.77 mm
- net VIN: track 45.1 -> 47.1 mm
- net USB_DP: track 11.5 -> 13.1 mm
- net +3V3: track 69.6 -> 70.7 mm
- net FLASH_CS: track 33.9 -> 34.7 mm
- net +1V8: track 36.0 -> 35.3 mm
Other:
- board text added: "FPGA Core Board ve3"
- board text removed: "FPGA Core Board ver2.1"

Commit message: 微修正
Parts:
- removed D1: USB, my_rcl:SOD123
- added FB9: USB, my_rcl:1608-J
- moved IC6 1.77 mm to (14.0, -19.5)
- moved C1 1.75 mm to (3.50, -23.0)
- moved CON3 1.68 mm to (14.0, -20.2)
- moved R11 1.67 mm to (11.1, -23.1)
- moved C44 1.64 mm to (17.5, -23.1)
- moved R16 1.25 mm to (-16.5, -15.0)
- moved R20 1.25 mm to (-18.2, -15.0)
- moved R15 0.90 mm to (-14.0, -15.8), turned to 0 degrees
- moved C41 0.35 mm to (6.00, -2.50)
- moved D2 0.25 mm to (-10.2, -11.5)
- moved D3 0.25 mm to (-12.0, -11.5)
- moved D4 0.25 mm to (-13.8, -11.5)
- moved D5 0.25 mm to (-15.5, -11.5)
- moved D6 0.25 mm to (-17.2, -11.5)
- moved J3 0.25 mm to (6.50, -9.50)
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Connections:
- net USB_+5V: now also FB9.1; no longer D1.1
- net VIN: now also FB9.2; no longer D1.2
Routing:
- net VIN: track 47.1 -> 38.6 mm, vias 1 -> 3
- net +3V3: track 70.7 -> 63.0 mm, vias 23 -> 25
- net GND: track 0.00 -> 4.14 mm, vias 153 -> 156
- net FLASH_MISO: track 31.3 -> 34.4 mm
- net N$7: track 9.98 -> 12.8 mm, vias 2 -> 1
- net N$4: track 1.70 -> 4.00 mm
- net N$6: track 9.88 -> 12.2 mm, vias 2 -> 1
- net FLASH_CS: track 34.7 -> 36.7 mm
- net USB_DM: track 11.8 -> 13.8 mm
- net FLASH_SCK: track 37.9 -> 39.7 mm
- net USB_+5V: track 9.90 -> 11.6 mm, vias 4 -> 3
- net FLASH_MOSI: track 25.3 -> 26.8 mm
- net USB_DP: track 13.1 -> 14.5 mm
